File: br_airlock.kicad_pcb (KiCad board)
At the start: 2 copper layers, 17.8 x 43.2 mm, 6 parts, among them P1 Digital, P2 Analog, P3 CONN_01X01, P4 CONN_01X01, P5 CONN_01X01, P6 CONN_01X01

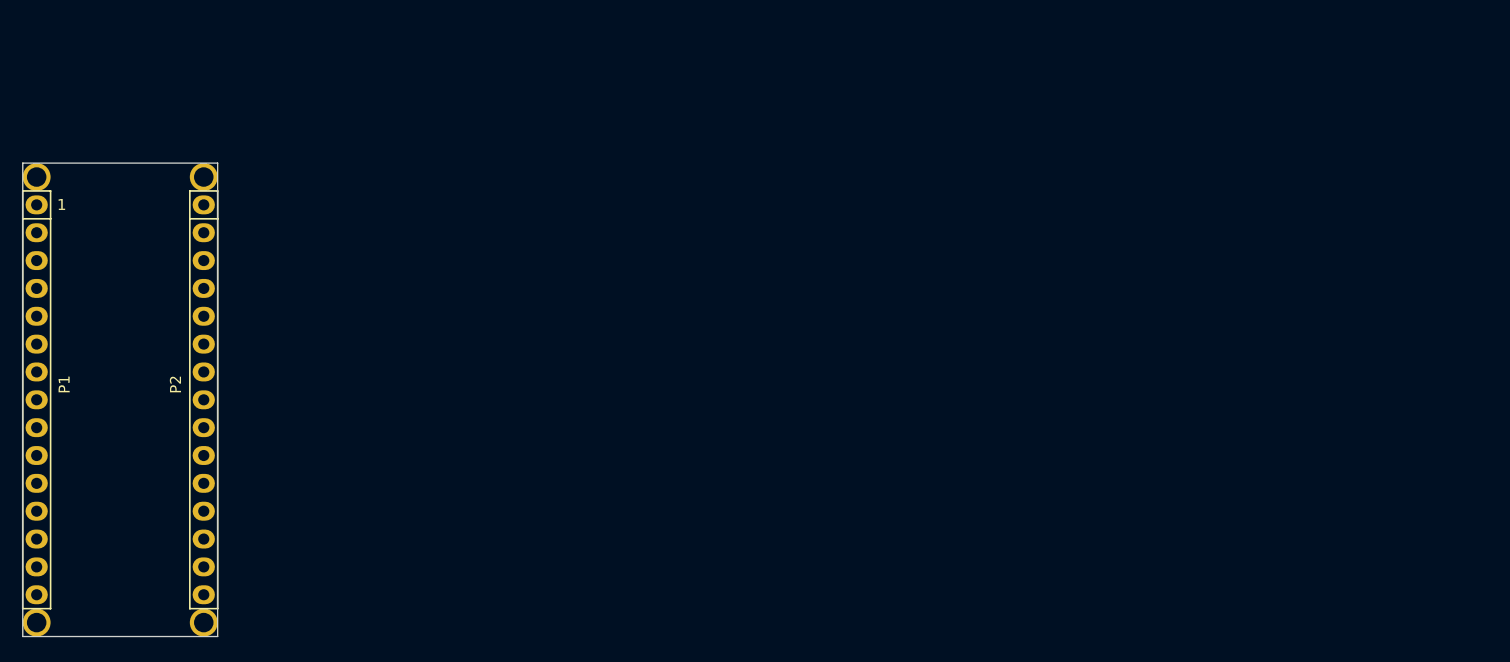
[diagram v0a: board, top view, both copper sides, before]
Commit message: More work. Relay needs looking at, and a VERY rough visualisation of a PCB
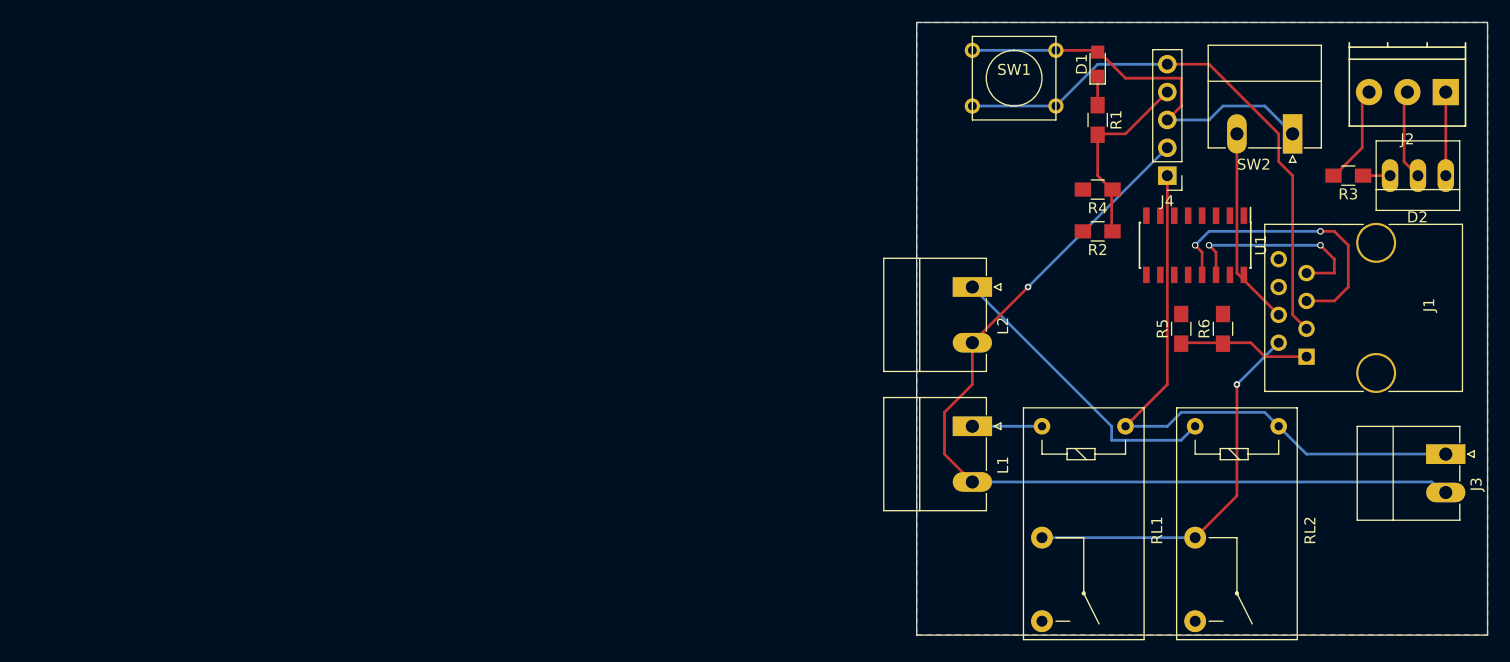
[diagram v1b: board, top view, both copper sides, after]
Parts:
- removed P1: Digital, Socket_Arduino_Nano:Socket_Strip_Arduino_1x15
- removed P2: Analog, Socket_Arduino_Nano:Socket_Strip_Arduino_1x15
- removed P3, P4, P5, P6: CONN_01X01, Socket_Arduino_Nano:1pin_Nano
- added D1: Power, LEDs:LED_0805, F.Cu at (236.2, 58.4)
- added D2: LED_Dual_AAC, Connectors:PINHEAD1-3, F.Cu at (268.0, 68.6)
- added J1: RJ45_LEDS, Connectors:RJ45_8, F.Cu at (255.3, 85.1)
- added J2: LEDS, Connectors_Terminal_Blocks:TerminalBlock_Pheonix_PT-3.5mm_3pol, F.Cu at (268.0, 61.0)
- added J3: 24v Power, Connectors_Phoenix:PhoenixContact_MC-G_02x3.50mm_Angled, F.Cu at (268.0, 94.0)
- added J4: CONN_01X05, Pin_Headers:Pin_Header_Straight_1x05_Pitch2.54mm, F.Cu at (242.6, 68.6)
- added L1: Magnet Plate, Connectors_Phoenix:PhoenixContact_MC-G_02x5.08mm_Angled, F.Cu at (224.8, 91.4)
- added L2: Door Strike, Connectors_Phoenix:PhoenixContact_MC-G_02x5.08mm_Angled, F.Cu at (224.8, 78.7)
- added R1: R, Resistors_SMD:R_0805_HandSoldering, F.Cu at (236.2, 63.5)
- added R2: R, Resistors_SMD:R_0805_HandSoldering, F.Cu at (236.2, 73.7)
- added R3: R, Resistors_SMD:R_0805_HandSoldering, F.Cu at (259.1, 68.6)
- added R4: R, Resistors_SMD:R_0805_HandSoldering, F.Cu at (236.2, 69.8)
- added R5: R, Resistors_SMD:R_0805_HandSoldering, F.Cu at (243.8, 82.5)
- added R6: R, Resistors_SMD:R_0805_HandSoldering, F.Cu at (247.7, 82.5)
- added RL1: FINDER-36.11-4301, BR_relay:Relay_SPST-NO_OMRON-G5Q, F.Cu at (231.1, 91.4)
- added RL2: FINDER-36.11-4301, BR_relay:Relay_SPST-NO_OMRON-G5Q, F.Cu at (245.1, 91.4)
- added SW1: Door Release, Buttons_Switches_THT:SW_PUSH_SMALL, F.Cu at (228.6, 59.7)
- added SW2: SW_Reed, Connectors_Phoenix:PhoenixContact_MC-G_02x5.08mm_Angled, F.Cu at (254.0, 64.8)
- added U1: PCF8574, Housings_SOIC:SOIC-16_3.9x9.9mm_Pitch1.27mm, F.Cu at (245.1, 74.9)
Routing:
- net GNDA: track 0.00 -> 84.0 mm, vias 0 -> 1
- net GND: track 0.00 -> 61.9 mm, vias 0 -> 1
- net +24V: track 0.00 -> 55.8 mm
- net DO_Open_Req: track 0.00 -> 51.0 mm
- net VCC: track 0.00 -> 50.0 mm
- net Net-(L2-Pad1): track 0.00 -> 27.4 mm
- net Net-(J1-Pad5): track 0.00 -> 26.1 mm, vias 0 -> 2
- net Net-(J1-Pad7): track 0.00 -> 18.7 mm, vias 0 -> 2
- net Net-(J1-Pad12): track 0.00 -> 18.1 mm
- net Net-(D2-Pad2): track 0.00 -> 8.46 mm
- net Net-(D2-Pad1): track 0.00 -> 7.62 mm
- net Net-(L1-Pad1): track 0.00 -> 6.35 mm
- net Net-(D1-Pad1): track 0.00 -> 2.63 mm
- net Net-(D2-Pad3): track 0.00 -> 2.46 mm
- added copper zone on F.Cu, net GND
- added copper zone on B.Cu, net VCC
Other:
- board size 17.8 x 43.2 mm -> 52.1 x 55.9 mm
- board text removed: "1"
